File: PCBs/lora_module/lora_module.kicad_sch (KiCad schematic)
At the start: 1 part, among them U101 Watch_Module_Outline_V1

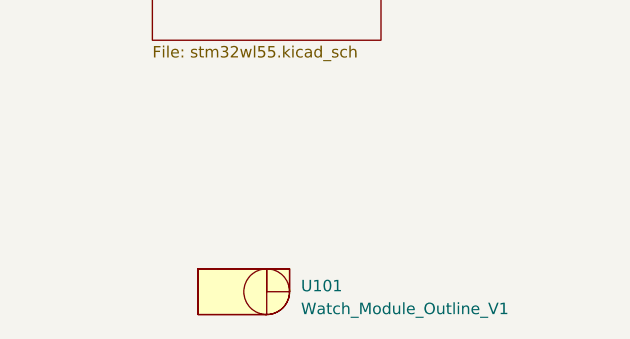
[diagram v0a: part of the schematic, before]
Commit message: RFID Module v1.1 complete (+default firmware)
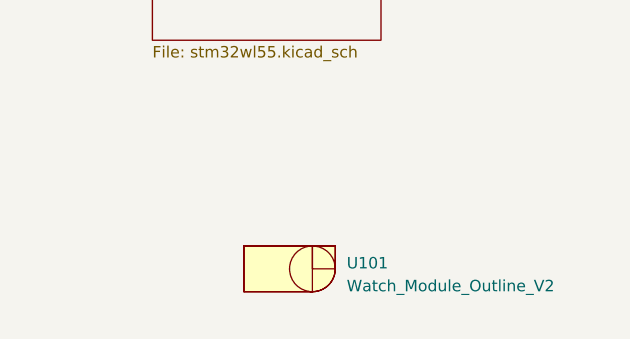
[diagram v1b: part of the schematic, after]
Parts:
- removed U101: Watch_Module_Outline_V1, watch_footprints:Watch Module Outline V1, symbol watch_symbols_lib:Watch_Module_Outline_V1
- added U101: Watch_Module_Outline_V2, watch_footprints:Watch Module Outline V2, symbol watch_symbols_lib:Watch_Module_Outline_V2
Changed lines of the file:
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@@
 (kicad_sch (version 20230121) (generator eeschema)
   (paper "A4")
-  (symbol (lib_id "watch_symbols_lib:Watch_Module_Outline_V1") (at 137.16 129.54 0) (unit 1)
+  (symbol (lib_id "watch_symbols_lib:Watch_Module_Outline_V2") (at 142.24 127 0) (unit 1)
     (in_bom no) (on_board yes) (dnp no) (fields_autoplaced)
-    (property "Reference" "U101" (at 143.51 128.905 0)
+    (property "Reference" "U101" (at 148.59 126.365 0)
       (effects (font (size 1.27 1.27)) (justify left))
     )
-    (property "Value" "Watch_Module_Outline_V1" (at 143.51 131.445 0)
+    (property "Value" "Watch_Module_Outline_V2" (at 148.59 128.905 0)
       (effects (font (size 1.27 1.27)) (justify left))
     )
-    (property "Footprint" "watch_footprints:Watch Module Outline V1" (at 137.16 134.62 0)
+    (property "Footprint" "watch_footprints:Watch Module Outline V2" (at 142.24 132.08 0)
       (effects (font (size 1.27 1.27)) hide)
     )
-    (property "Datasheet" "" (at 137.16 129.54 0)
+    (property "Datasheet" "" (at 142.24 127 0)
       (effects (font (size 1.27 1.27)) hide)
     )
     (instances
-      (project "rfid_module"
-        (path "/7f374643-2d66-4cfc-a525-255f058de0be"
-          (reference "U101") (unit 1)
-        )
-      )
       (project "lora_module"
         (path "/d37a0b00-acf2-4499-af5a-9e1daf93b8f4"
